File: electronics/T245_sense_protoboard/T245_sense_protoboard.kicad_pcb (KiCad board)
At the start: 2 copper layers, 2 parts

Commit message: WIP placement
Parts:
- added C1: 1u, SquantorCapacitor:C_0603, B.Cu at (78.7, 50.8)
- added C2: 1u, SquantorCapacitor:C_0603, B.Cu at (85.1, 34.3)
- added C3: 1u, SquantorCapacitor:C_0603, B.Cu at (88.9, 38.1)
- added C4: 1u, SquantorCapacitor:C_0603, B.Cu at (95.2, 36.8)
- added C5: 1u, SquantorCapacitor:C_0603, B.Cu at (106.7, 50.8)
- added C6: 1u, SquantorCapacitor:C_0603, B.Cu at (108.0, 41.9)
- added C7: 1u, SquantorCapacitor:C_0603, B.Cu at (102.9, 54.6)
- added C8: 1u, SquantorCapacitor:C_0603, B.Cu at (88.9, 58.4)
- added C9: 1u, SquantorCapacitor:C_0603, B.Cu at (95.2, 57.1)
- added D1: ~, SquantorIC:SOT23-3, B.Cu at (108.0, 40.6)
- added D2: ~, SquantorIC:SOT23-3, B.Cu at (102.9, 55.9)
- added J1: Conn_01x06, Connector_Molex:Molex_KK-254_AE-6410-06A_1x06_P2.54mm_Vertical, F.Cu at (132.1, 25.4)
- added J2: Conn_02x03_Odd_Even, Connector_Molex:Molex_Micro-Fit_3.0_43045-0612_2x03_P3.00mm_Vertical, F.Cu at (64.2, 38.9)
- added R1: 22K6, SquantorResistor:R_0603_hand, B.Cu at (77.5, 44.5)
- added R10: 22K6, SquantorResistor:R_0603_hand, B.Cu at (105.4, 44.5)
- added R11: 10K, SquantorResistor:R_0603_hand, B.Cu at (99.1, 53.3)
- added R12: 10K, SquantorResistor:R_0603_hand, B.Cu at (101.6, 50.8)
- added R13: 187K, SquantorResistor:R_0603_hand, B.Cu at (102.9, 52.1)
- added R14: 3K3, SquantorResistor:R_0603_hand, B.Cu at (104.1, 53.3)
- added R15: 2K2, SquantorResistor:R_0603_hand, B.Cu at (106.7, 43.2)
- added R16: 200K, SquantorResistor:R_0603_hand, B.Cu at (90.2, 59.7)
- added R17: 200K, SquantorResistor:R_0603_hand, B.Cu at (90.2, 57.1)
- added R18: 4k75, SquantorResistor:R_0603_hand, B.Cu at (87.6, 57.1)
- added R19: 4k75, SquantorResistor:R_0603_hand, B.Cu at (87.6, 59.7)
- added R2: 22K6, SquantorResistor:R_0603_hand, B.Cu at (77.5, 39.4)
- added R20: 0R22, SquantorResistor:R_0805, B.Cu at (85.1, 57.1)
- added R21: 0R22, SquantorResistor:R_0805, B.Cu at (85.1, 59.7)
- added R3: 22K6, SquantorResistor:R_0603_hand, B.Cu at (77.5, 36.8)
- added R4: 22K6, SquantorResistor:R_0603_hand, B.Cu at (77.5, 34.3)
- added R5: 590K, SquantorResistor:R_0603_hand, B.Cu at (90.2, 39.4)
- added R6: 590K, SquantorResistor:R_0603_hand, B.Cu at (90.2, 36.8)
- added R7: 82K, SquantorResistor:R_0603_hand, B.Cu at (95.2, 34.3)
- added R8: 2K7, SquantorResistor:R_0603_hand, B.Cu at (101.6, 43.2)
- added R9: 2K7, SquantorResistor:R_0603_hand, B.Cu at (104.1, 45.7)
- added U1: ~, Package_DIP:DIP-16_W7.62mm, F.Cu at (78.7, 34.3)
- added U2: OP07C, Package_DIP:DIP-8_W7.62mm, F.Cu at (88.9, 34.3)
- added U3: LM358, Package_DIP:DIP-8_W7.62mm, F.Cu at (106.7, 44.5)
- added U4: OP07C, Package_DIP:DIP-8_W7.62mm, F.Cu at (88.9, 54.6)
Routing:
- net /-5V: track 0.00 -> 44.5 mm, vias 0 -> 1
- net GND: track 0.00 -> 43.3 mm
- net /SEN-: track 0.00 -> 12.3 mm
- net Net-(U4-OUT): track 0.00 -> 6.55 mm, vias 0 -> 1
- net Net-(U2-OUT): track 0.00 -> 6.55 mm, vias 0 -> 1
- net /+8V: track 0.00 -> 6.35 mm
- net /SEN+: track 0.00 -> 3.59 mm
- net /+3.3V: track 0.00 -> 1.27 mm
- net (no net): vias 0 -> 2

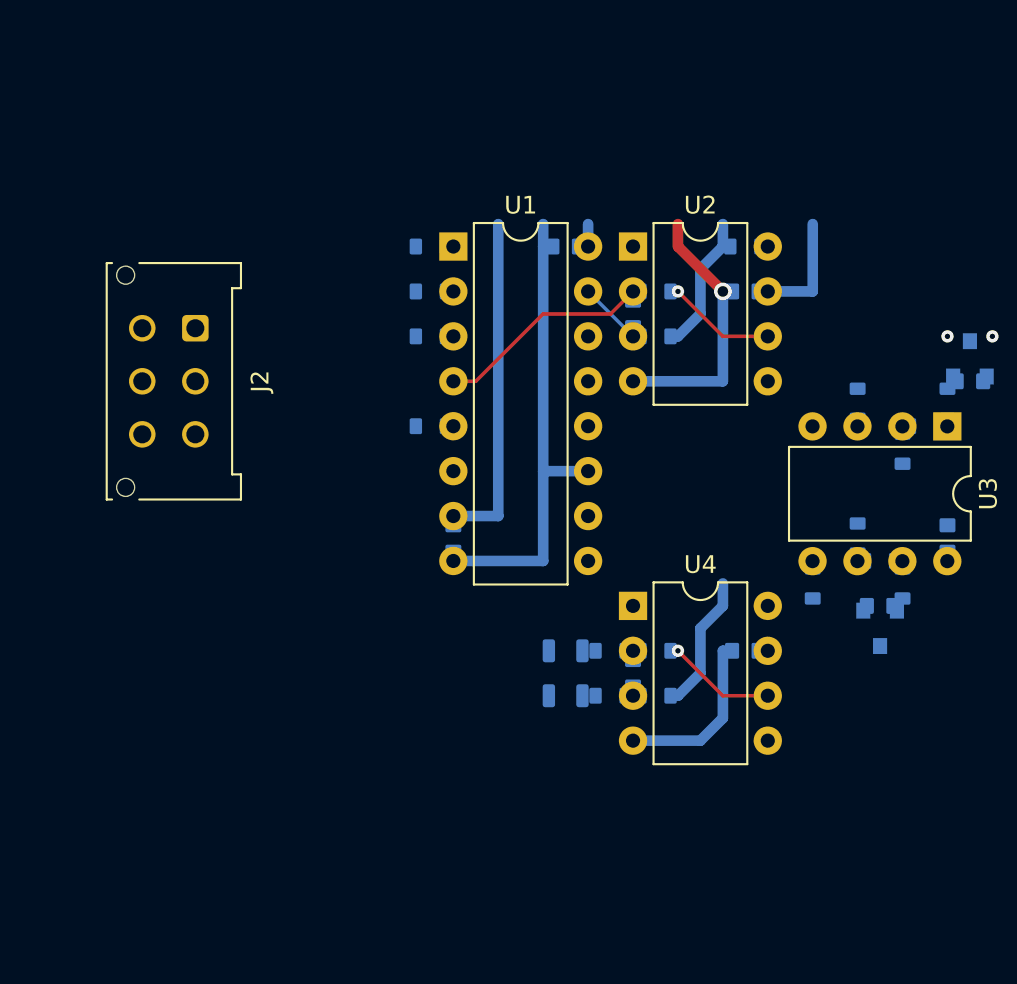
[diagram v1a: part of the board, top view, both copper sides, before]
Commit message: switched to dual mux for experiments
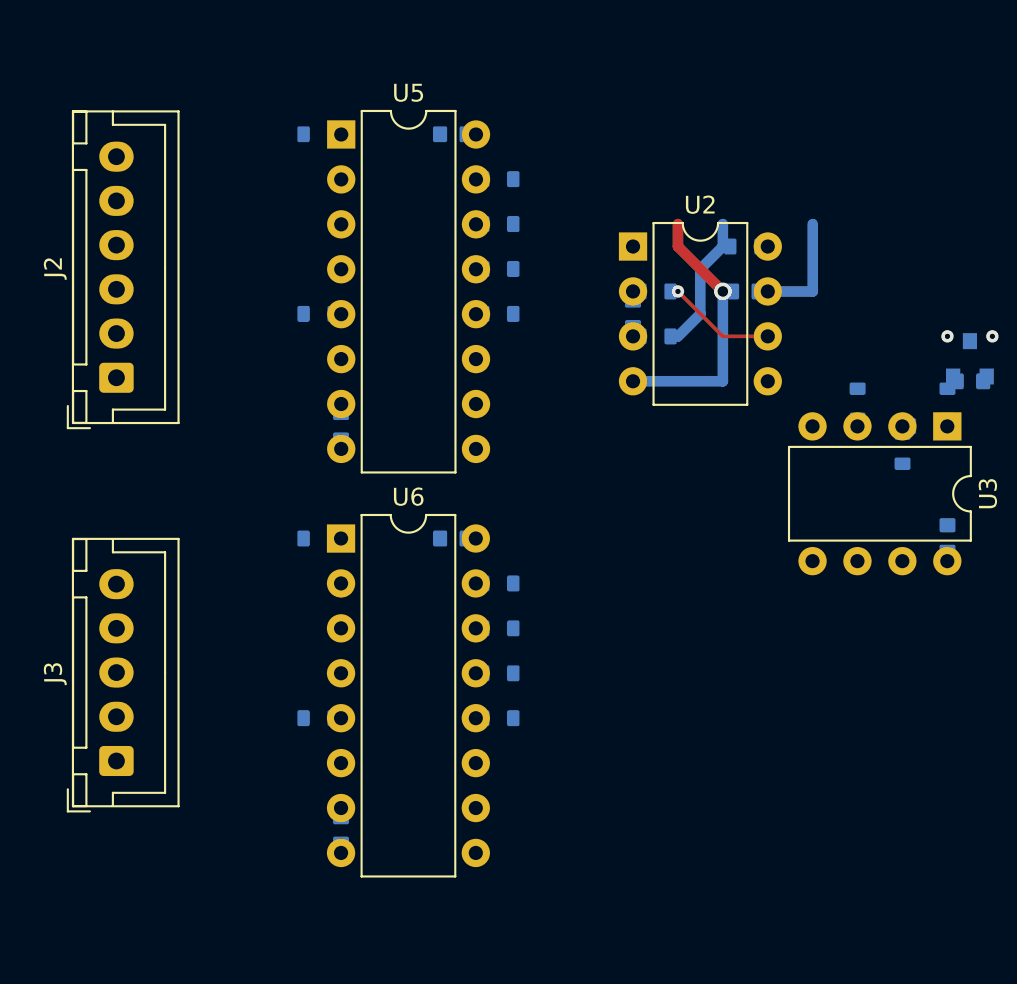
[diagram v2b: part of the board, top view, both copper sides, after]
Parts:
- removed C7, C8, C9: 1u, SquantorCapacitor:C_0603
- removed D2: ~, SquantorIC:SOT23-3
- removed R11, R12: 10K, SquantorResistor:R_0603_hand
- removed R13: 187K, SquantorResistor:R_0603_hand
- removed R14: 3K3, SquantorResistor:R_0603_hand
- removed R16, R17: 200K, SquantorResistor:R_0603_hand
- removed R18, R19: 4k75, SquantorResistor:R_0603_hand
- removed R20, R21: 0R22, SquantorResistor:R_0805
- removed U1: ~, Package_DIP:DIP-16_W7.62mm
- removed U4: OP07C, Package_DIP:DIP-8_W7.62mm
- added C10: 1u, SquantorCapacitor:C_0603, B.Cu at (78.7, 50.8)
- added C11: 1u, SquantorCapacitor:C_0603, B.Cu at (72.4, 67.3)
- added J3: Conn_01x05, Connector_JST:JST_XH_B5B-XH-A_1x05_P2.50mm_Vertical, F.Cu at (59.7, 63.4)
- added R22: 22K6, SquantorResistor:R_0603_hand, B.Cu at (81.3, 35.6)
- added R23: 22K6, SquantorResistor:R_0603_hand, B.Cu at (81.3, 33.0)
- added R24: 22K6, SquantorResistor:R_0603_hand, B.Cu at (81.3, 30.5)
- added R25: 22K6, SquantorResistor:R_0603_hand, B.Cu at (81.3, 53.3)
- added R26: 22K6, SquantorResistor:R_0603_hand, B.Cu at (81.3, 55.9)
- added R27: 22K6, SquantorResistor:R_0603_hand, B.Cu at (81.3, 58.4)
- added R28: 22K6, SquantorResistor:R_0603_hand, B.Cu at (71.1, 27.9)
- added R29: 22K6, SquantorResistor:R_0603_hand, B.Cu at (71.1, 38.1)
- added U5: 74XX4051, Package_DIP:DIP-16_W7.62mm, F.Cu at (72.4, 28.0)
- added U6: 74XX4051, Package_DIP:DIP-16_W7.62mm, F.Cu at (72.4, 50.8)
- J2: value Conn_02x03_Odd_Even -> Conn_01x06; footprint Connector_Molex:Molex_Micro-Fit_3.0_43045-0612_2x03_P3.00mm_Vertical -> Connector_JST:JST_XH_B6B-XH-A_1x06_P2.50mm_Vertical
- moved R3 25.0 mm to (71.1, 61.0), turned to 180 degrees
- moved R1 16.9 mm to (81.3, 61.0), turned to 180 degrees
- moved R2 13.1 mm to (71.1, 50.8), turned to 180 degrees
- moved C2 8.98 mm to (78.7, 27.9)
- moved C1 8.98 mm to (72.4, 44.5)
- moved R4 5.39 mm to (81.3, 38.1), turned to 180 degrees
- moved J2 5.27 mm to (59.7, 41.7), turned to 90 degrees
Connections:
- R1 pad 1: /TC -> /LOAD_2
- R2 pad 1: /LOAD -> Net-(U6-A4)
- R2 pad 2: Net-(U1-C1) -> /COM_2
- R3 pad 1: /COM -> Net-(U6-A5)
- R3 pad 2: Net-(U1-B0) -> /TC_2
- R4 pad 1: /TC -> /LOAD_2
- U3 pad 5: Net-(U3-+IN2) -> GND
- U3 pad 7: Net-(U3-OUT2) -> Net-(U3--IN2)
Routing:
- net GND: track 43.3 -> 8.24 mm
- net /-5V: track 44.5 -> 15.5 mm
- net /SEN-: track 12.3 -> 0.00 mm
- net Net-(U4-OUT): track 6.55 -> 0.00 mm, vias 1 -> 0
- net /SEN+: track 3.59 -> 0.00 mm
- net /+3.3V: track 1.27 -> 0.00 mm

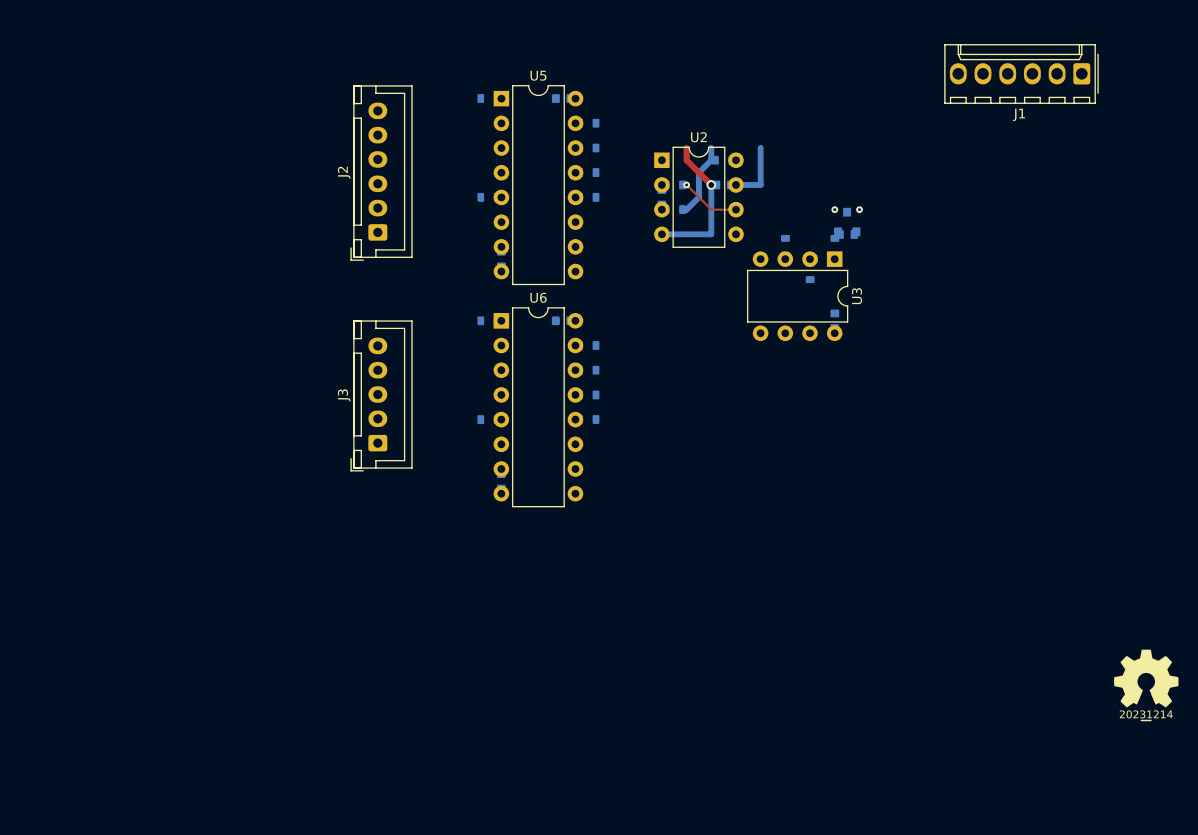
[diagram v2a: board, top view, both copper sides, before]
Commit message: switched mux pinning and additional placing
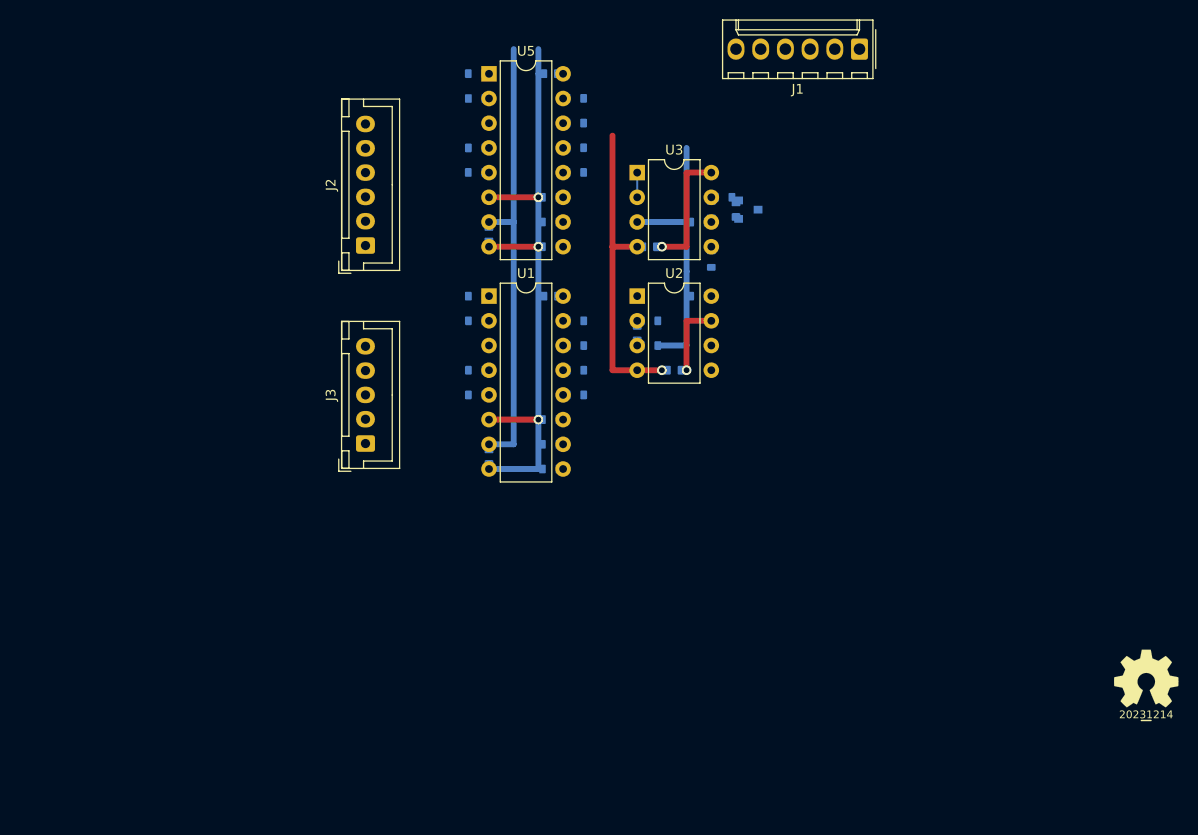
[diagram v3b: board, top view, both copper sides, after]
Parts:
- removed C10, C11: 1u, SquantorCapacitor:C_0603
- removed U6: 74XX4051, Package_DIP:DIP-16_W7.62mm
- added C7: 1u, SquantorCapacitor:C_0603, B.Cu at (77.5, 48.3)
- added C8: 1u, SquantorCapacitor:C_0603, B.Cu at (71.1, 64.8)
- added R11: 22K6, SquantorResistor:R_0603_hand, B.Cu at (69.8, 27.9)
- added R12: 22K6, SquantorResistor:R_0603_hand, B.Cu at (69.8, 33.0)
- added R13: 22K6, SquantorResistor:R_0603_hand, B.Cu at (69.8, 58.4)
- added R14: 22K6, SquantorResistor:R_0603_hand, B.Cu at (80.0, 50.8)
- added R16: 22K6, SquantorResistor:R_0603_hand, B.Cu at (80.0, 53.3)
- added R17: 22K6, SquantorResistor:R_0603_hand, B.Cu at (80.0, 55.9)
- added R18: 22K6, SquantorResistor:R_0603_hand, B.Cu at (80.0, 58.4)
- added R19: 47K, SquantorResistor:R_0603_hand, B.Cu at (77.5, 38.1)
- added R20: 47K, SquantorResistor:R_0603_hand, B.Cu at (77.5, 40.6)
- added R21: 47K, SquantorResistor:R_0603_hand, B.Cu at (77.5, 43.2)
- added U1: 74XX4051, Package_DIP:DIP-16_W7.62mm, F.Cu at (71.1, 48.3)
- R25, R26, R27: value 22K6 -> 47K
- moved J1 23.0 mm to (109.2, 22.9)
- moved U3 22.2 mm to (86.4, 35.6), turned to 0 degrees
- moved C5 20.5 mm to (87.6, 43.2), turned to 180 degrees
- moved C4 19.7 mm to (90.2, 55.9)
- moved R1 17.1 mm to (69.8, 48.3)
- moved R5 14.2 mm to (87.6, 53.3)
- moved C3 14.2 mm to (86.4, 52.1)
- moved R6 14.2 mm to (87.6, 50.8)
- moved R7 14.2 mm to (92.7, 48.3)
- moved U2 14.2 mm to (86.4, 48.3)
- moved R15 12.5 mm to (95.2, 38.1), turned to 180 degrees
- moved R10 12.5 mm to (94.0, 39.4), turned to 90 degrees
- moved R9 12.5 mm to (92.7, 40.6), turned to 0 degrees
- moved C6 11.7 mm to (96.5, 39.4), turned to -90 degrees
- moved D1 10.2 mm to (97.8, 39.4), turned to 0 degrees
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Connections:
- net /HDL3 renamed /1_HDL3
- net /HDL4 renamed /1_HDL4
- net /HDL6 renamed /1_HDL6
- J2 pad 1: /TC -> /1_TC
- J2 pad 2: /COM -> /1_COM
- J2 pad 5: /LOAD -> /1_LOAD
- J3 pad 1: unconnected-(J3-Pin_1-Pad1) -> /2_C1
- J3 pad 2: unconnected-(J3-Pin_2-Pad2) -> /2_C3B
- J3 pad 3: unconnected-(J3-Pin_3-Pad3) -> /2_C2
- J3 pad 4: unconnected-(J3-Pin_4-Pad4) -> /2_C3A
- J3 pad 5: unconnected-(J3-Pin_5-Pad5) -> /2_Sense
- R1 pad 1: /LOAD_2 -> Net-(U1-A4)
- R1 pad 2: Net-(U6-A3) -> /2_C2
- R10 pad 1: Net-(U3--IN1) -> Net-(U3--IN2)
- R10 pad 2: Net-(U3-OUT1) -> Net-(U3-OUT2)
- R15 pad 2: Net-(U3-OUT1) -> Net-(U3-OUT2)
- R2 pad 2: /COM_2 -> unconnected-(R2-Pad2)
- R22 pad 1: /TC -> /1_TC
- R23 pad 1: /COM -> /1_LOAD
- R24 pad 1: /LOAD -> /2_C1
- R25 pad 1: /LOAD -> /MUX1_0
- R25 pad 2: Net-(U6-A2) -> GND
- R26 pad 1: /COM -> /MUX1_1
- R26 pad 2: Net-(U6-A1) -> GND
- R27 pad 1: /TC -> /MUX1_2
- R27 pad 2: Net-(U6-A0) -> GND
- R28 pad 2: /COM_2 -> /2_C2
- R29 pad 2: /TC_2 -> /2_C3A
- R3 pad 2: /TC_2 -> unconnected-(R3-Pad2)
- R4 pad 1: /LOAD_2 -> /2_C3B
- R8 pad 2: Net-(U3-+IN1) -> Net-(U3-+IN2)
- R9 pad 2: Net-(U3--IN1) -> Net-(U3--IN2)
- U3 pad 1: Net-(U3-OUT1) -> Net-(U3--IN1)
- U3 pad 3: Net-(U3-+IN1) -> GND
- U3 pad 5: GND -> Net-(U3-+IN2)
- U3 pad 7: Net-(U3--IN2) -> Net-(U3-OUT2)
- U5 pad 2: unconnected-(U5-A6-Pad2) -> Net-(U5-A6)
- U5 pad 4: GND -> Net-(U5-A7)
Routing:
- net GND: track 8.24 -> 91.9 mm, vias 0 -> 3
- net /-5V: track 15.5 -> 78.0 mm
- net /+8V: track 6.35 -> 21.4 mm, vias 0 -> 2
- net Net-(U2-OUT): track 6.55 -> 0.00 mm, vias 1 -> 0
- net Net-(U3--IN1): track 0.00 -> 2.54 mm
- net (no net): vias 2 -> 0

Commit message: protoboard is now 1 on 1 copy of real protoboard
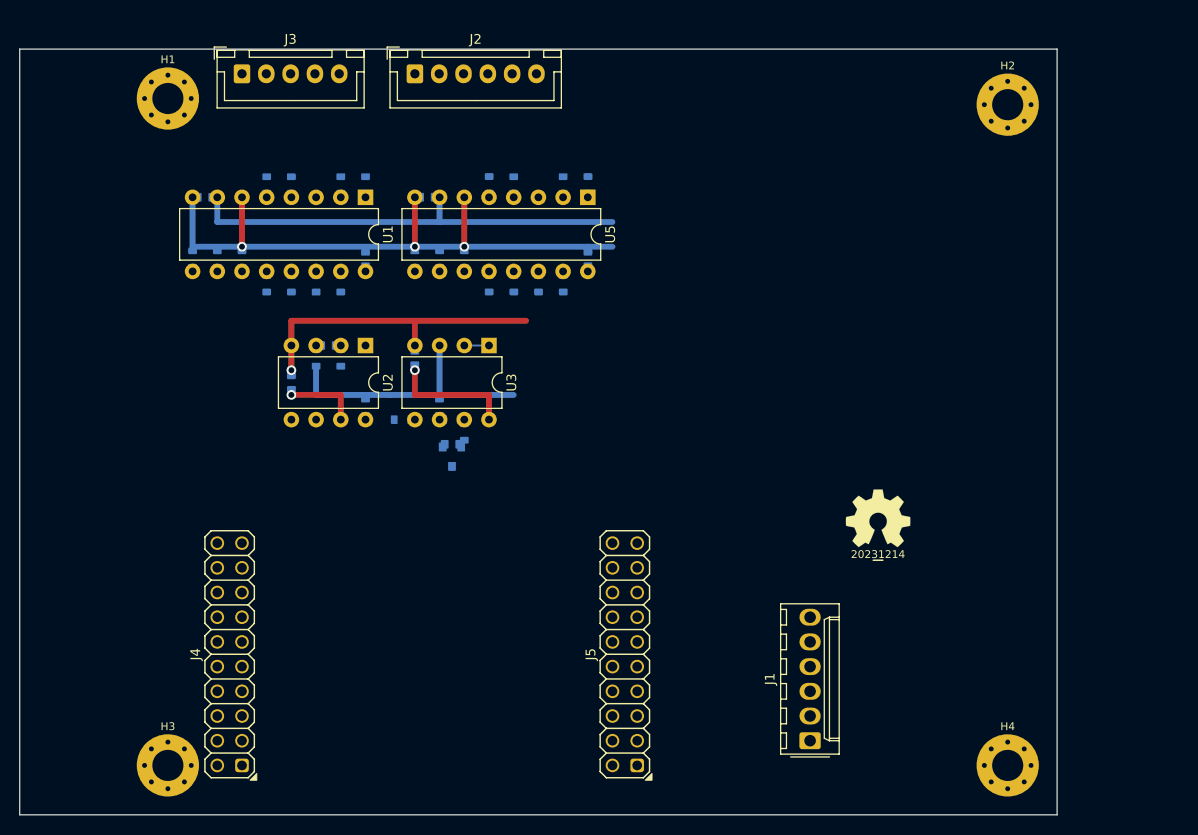
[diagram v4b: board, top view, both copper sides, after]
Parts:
- added H1: MountingHole, SquantorPcbOutline:MountingHole_3.2mm_M3_Pad_Via, F.Cu at (38.1, 27.9)
- added H2: MountingHole, SquantorPcbOutline:MountingHole_3.2mm_M3_Pad_Via, F.Cu at (124.5, 28.6)
- added H3: MountingHole, SquantorPcbOutline:MountingHole_3.2mm_M3_Pad_Via, F.Cu at (38.1, 96.5)
- added H4: MountingHole, SquantorPcbOutline:MountingHole_3.2mm_M3_Pad_Via, F.Cu at (124.5, 96.5)
- added J4: nuclone_left, SquantorConnectors:Header-0254-2X10-H010, F.Cu at (44.5, 85.1)
- added J5: nuclone_right, SquantorConnectors:Header-0254-2X10-H010, F.Cu at (85.1, 85.1)
- moved J1 71.3 mm to (104.1, 94.0), turned to 90 degrees
- moved R27 42.7 mm to (40.6, 44.5), turned to 90 degrees
- moved J3 40.1 mm to (45.7, 25.4), turned to 0 degrees
- moved D1 39.7 mm to (67.3, 64.8), turned to -90 degrees
- moved C8 39.6 mm to (41.9, 38.1), turned to 0 degrees
- moved C4 39.4 mm to (50.8, 57.1), turned to 90 degrees
- moved R26 39.2 mm to (43.2, 44.5), turned to 90 degrees
- moved C6 37.9 mm to (67.3, 63.5), turned to 180 degrees
- moved R7 36.1 mm to (58.4, 59.7), turned to -90 degrees
- moved R15 36.0 mm to (68.6, 62.2), turned to 90 degrees
- moved R25 35.8 mm to (45.7, 44.5), turned to 90 degrees
- moved R8 35.8 mm to (62.2, 61.0), turned to 0 degrees
- moved R10 34.3 mm to (67.3, 61.0), turned to 0 degrees
- moved R5 34.3 mm to (53.3, 54.6), turned to 90 degrees
- moved R18 33.7 mm to (48.3, 47.0), turned to 90 degrees
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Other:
- board outline added: 106.7 x 78.7 mm
